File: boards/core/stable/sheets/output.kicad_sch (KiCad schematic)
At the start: 21 parts, among them U216 NE5532, U217 TL072

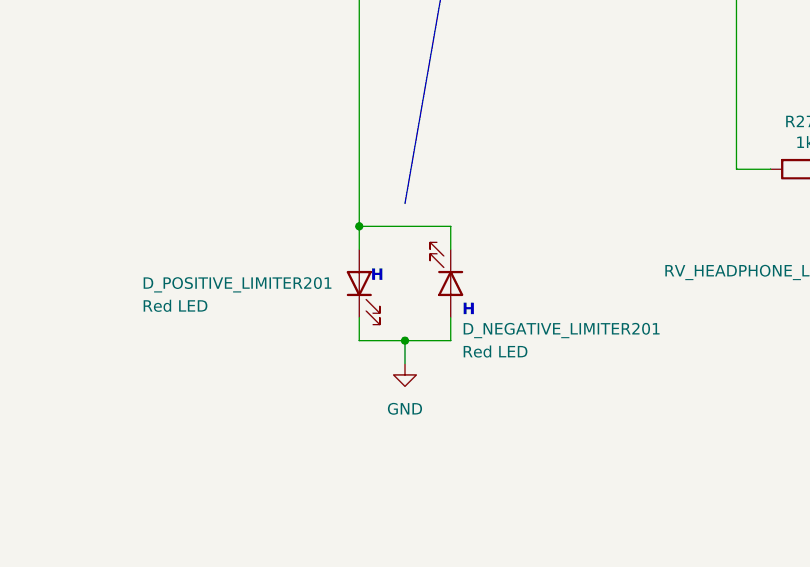
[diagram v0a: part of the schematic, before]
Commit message: Updated and checked Core board BOM
ref https://github.com/shmoergh/hog/issues/19
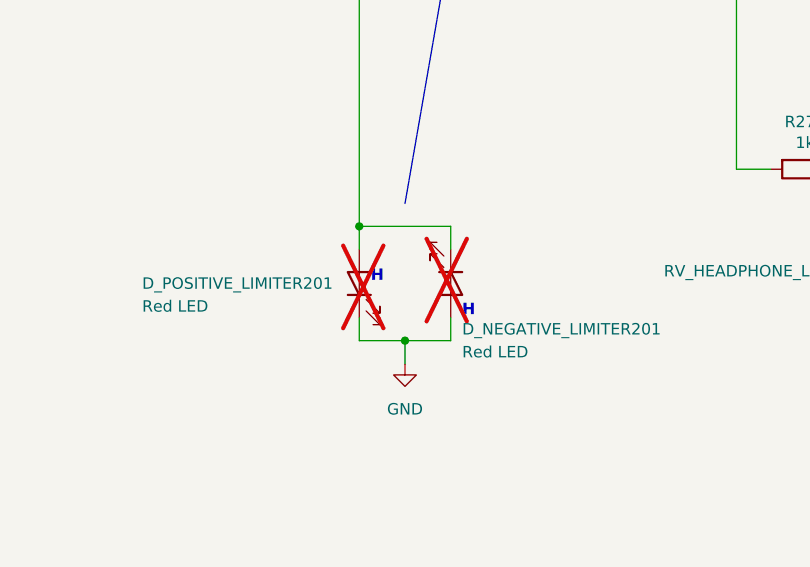
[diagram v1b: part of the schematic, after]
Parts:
- C203, C208, R201, R231, R271, R272, R273, R274, U216, U217: Vendor (none) -> JLCPCB
- D_NEGATIVE_LIMITER201, D_POSITIVE_LIMITER201: now not fitted
- RV_HEADPHONE_LIM201: Part No. (none) -> 531-PT6KH104A1010PM; Part URL (none) -> https://mou.sr/49zQlIS; Vendor (none) -> Mouser; now in the parts list
- RV_LINE_OUT_LVL201: Part No. (none) -> 531-PT6KH-10K; Part URL (none) -> https://mou.sr/4gcYhlU; Vendor (none) -> Mouser; now in the parts list
